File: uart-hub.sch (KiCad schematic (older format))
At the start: 21 parts, among them J2001 Stiftleiste 1x8, J2002 Buchsenleiste 1x6, horizontal, J2003 Stiftleiste 1x8, J2004 Buchsenleiste 1x6, horizontal, SW2001 DIP-Switch 8

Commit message: übergabe an 3ahel
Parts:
- removed J2001, J2003: Stiftleiste 1x8, Connector_PinHeader_2.54mm:PinHeader_1x08_P2.54mm_Vertical, symbol Connector:Conn_01x08_Male
- removed J2004: Buchsenleiste 1x6, horizontal, Connector_PinSocket_2.54mm:PinSocket_1x06_P2.54mm_Horizontal, symbol Connector_Generic:Conn_01x06
- removed R2001, R2002, R2005, R2007, R2009, R2010, R2013, R2015, R2016: 1k, Resistor_SMD:R_0603_1608Metric, symbol htl_passives:R_sig
- removed R2011, R2012, R2014: 100R, Resistor_SMD:R_0603_1608Metric, symbol htl_passives:R_sig
- added J2001, J2002: Stiftleiste 2x9, Connector_PinHeader_2.54mm:PinHeader_2x09_P2.54mm_Vertical_SMD, symbol Connector_Generic:Conn_02x09_Odd_Even
- added R2001 (x2), R2002 (x2), R2003, R2005, R2007: 1k, Resistor_SMD:R_0603_1608Metric, symbol htl_passives:R_sig
- added R2004, R2005, R2006, R2007, R2008: 100R, Resistor_SMD:R_0603_1608Metric, symbol htl_passives:R_sig
- R2003, R2004, R2006: DistOrderNr (none) -> C25201; Distributor (none) -> LCSC; ManPartNr (none) -> 0603WAJ0101T5E; Manufacturer (none) -> UNI-ROYAL; Notes (none) -> 100R, 5%, 100mW; PriceEUR (none) -> 0.000563; PriceForQty (none) -> 1000; Weblink (none) -> https://lcsc.com/product-detail/Chip-Resistor-Surface-Mount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
- R2008: DistOrderNr (none) -> C103209; Distributor (none) -> LCSC; ManPartNr (none) -> RTT03102JTP; Manufacturer (none) -> RALEC; Notes (none) -> 1kΩ ±5% 0.1W ±100ppm/℃; PriceEUR (none) -> 0.000556; PriceForQty (none) -> 1000; Weblink (none) -> https://lcsc.com/product-detail/Chip-Resistor-Surface-Mount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
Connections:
- net GND: now also J2001.17 (Pin_17), J2001.18 (Pin_18), J2002.17 (Pin_17), J2002.18 (Pin_18)
- net UART - RS232 1/UART_Rx1: now also SW2001.13, R2004.1; no longer SW2001.16
- net UART - RS232 1/UART_Rx2: now also SW2001.12, R2005.1; no longer SW2001.15
- net UART - RS232 1/UART_Tx1: now also SW2001.16, R2001.2; no longer SW2001.14
- net UART - RS232 1/UART_Tx2: now also SW2001.15, R2002.2; no longer SW2001.13
- net UART - RS232 2/UART_Rx1: now also SW2001.11, R2006.1; no longer SW2001.12
- net UART - RS232 2/UART_Rx2: now also R2007.1
- net UART - RS232 2/UART_Tx1: now also SW2001.14, R2003.2; no longer SW2001.11
- net USB - UART/RxD: now also SW2001.4, R2001.2; no longer SW2001.2
- net USB - UART/TxD: now also R2006.1, SW2001.1; no longer R2003.1, SW2001.3
- net USB - UART/~CTS: now also R2007.2
- net USB - UART/~DCD: now also SW2001.5, R2002.2; no longer SW2001.1
- net USB - UART/~DSR: now also SW2001.6, R2005.2; no longer SW2001.5
- net USB - UART/~DTR: now also R2003.1, SW2001.2; no longer R2004.1, SW2001.4
- net USB - UART/~RTR: now also R2004.1, SW2001.3; no longer R2006.1, SW2001.6
- net +3V3: now reaches SW2001.9
- net +3V3: now also R2008.1
- net at J2002.1 (Pin_1): now also R2003.2, J2001.3 (Pin_3), J2001.4 (Pin_4); no longer R2004.2
- net at J2002.2 (Pin_2): now also R2004.2, J2001.5 (Pin_5), J2001.6 (Pin_6); no longer R2006.2
- net at J2002.4 (Pin_4): now also J2001.7 (Pin_7), J2001.8 (Pin_8), R2001.1
- net at J2002.5 (Pin_5): now also R2006.2, J2001.1 (Pin_1), J2001.2 (Pin_2); no longer R2003.2
- net at R2008.1: now also J2001.15 (Pin_15), J2001.16 (Pin_16)
- new net: J2001.13 (Pin_13), J2001.14 (Pin_14), R2007.1
- new net: J2001.11 (Pin_11), J2001.12 (Pin_12), R2005.1
- new net: J2001.10 (Pin_10), J2001.9 (Pin_9), R2002.1
- new net: J2002.13 (Pin_13), J2002.14 (Pin_14), R2007.2
- new net: J2002.15 (Pin_15), J2002.16 (Pin_16), R2008.2
- new net: J2002.11 (Pin_11), J2002.12 (Pin_12), R2006.2
- new net: J2002.5 (Pin_5), J2002.6 (Pin_6), R2003.1
- new net: J2002.3 (Pin_3), J2002.4 (Pin_4), R2002.1
- new net: J2002.1 (Pin_1), J2002.2 (Pin_2), R2001.1
- new net: J2002.10 (Pin_10), J2002.9 (Pin_9), R2005.2
- new net: J2002.7 (Pin_7), J2002.8 (Pin_8), R2004.2
- no-connect marks 2 -> 1
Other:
- note added: "TxD\nDTR\nRTR\nRxD\nDCD\nDSR\nCTS\nRI"
- moved on the sheet: J2402

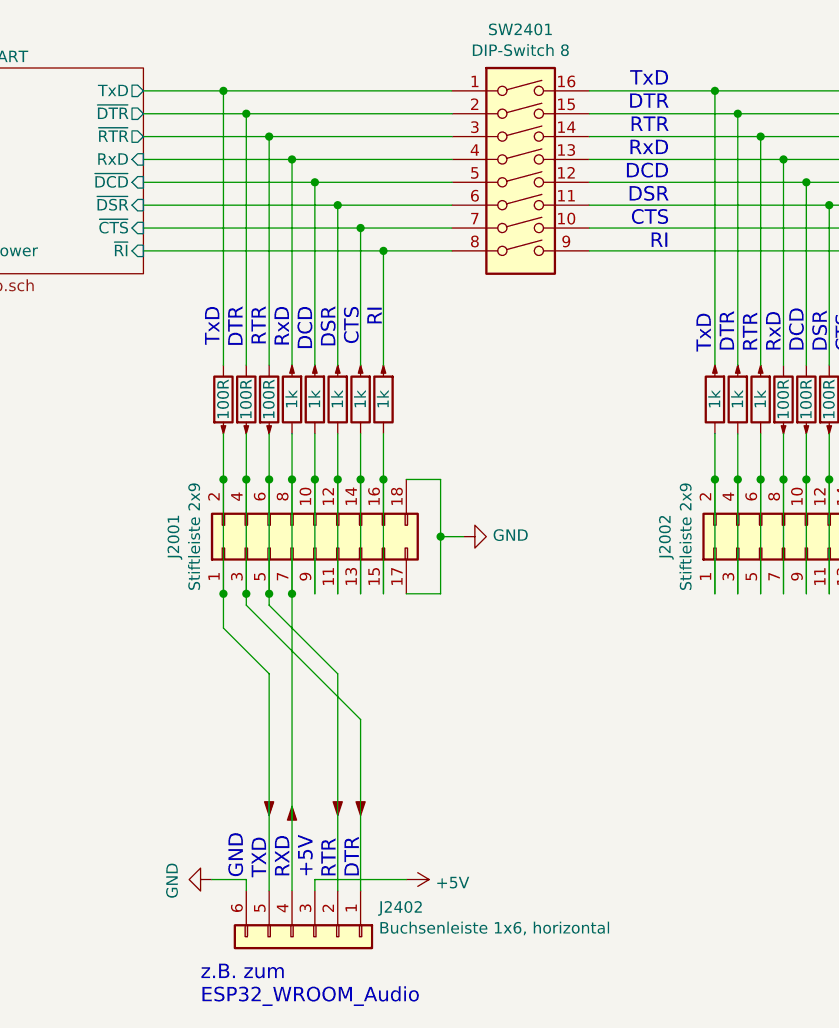
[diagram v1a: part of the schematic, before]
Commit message: Layout fast fertig Footprint für 2x9-polig wurde aktualisiert
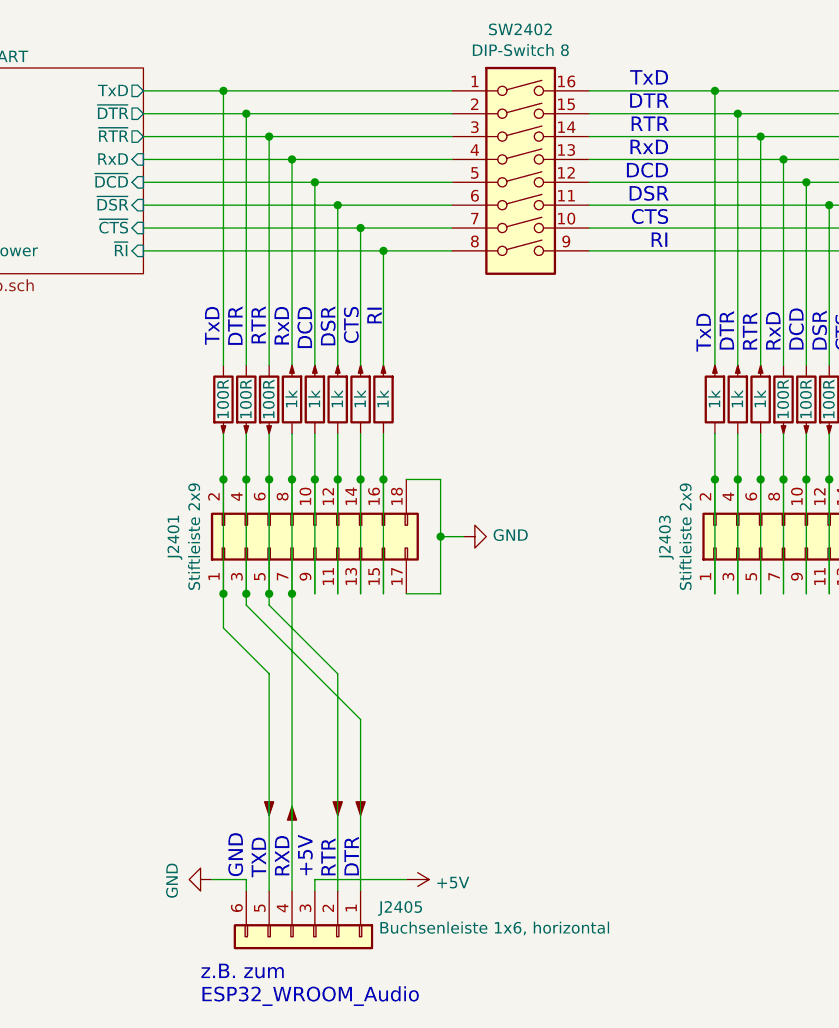
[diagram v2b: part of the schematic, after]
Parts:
- J2001, J2002: footprint Connector_PinHeader_2.54mm:PinHeader_2x09_P2.54mm_Vertical_SMD -> htl_connectors:PinHeader_2x09_P2.54mm_Vertical_SMD_LCSC_C88175
- J2002: footprint Connector_PinSocket_2.54mm:PinSocket_1x06_P2.54mm_Horizontal -> Connector_PinSocket_2.54mm:PinSocket_1x07_P2.54mm_Horizontal
